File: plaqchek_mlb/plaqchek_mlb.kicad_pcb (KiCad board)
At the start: 2 copper layers, 55 x 71 mm, 46 parts, among them J1 Conn_01x04, J2 Conn_01x04, J3 Conn_01x02, J5 Conn_01x04, SW1 SW_Push, SW2 SW_Push, SW3 SW_Push, U1 DHT22

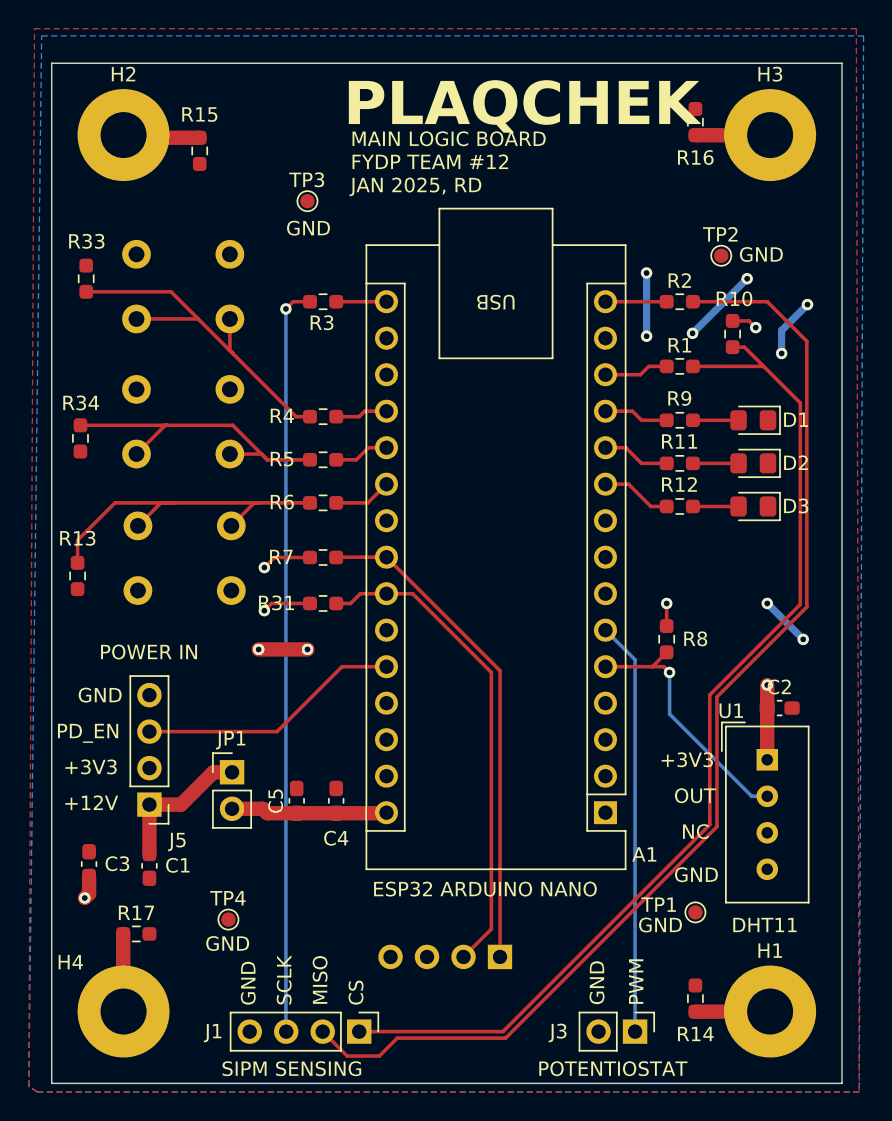
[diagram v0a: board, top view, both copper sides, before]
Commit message: finish potentiostat board, update board constraints
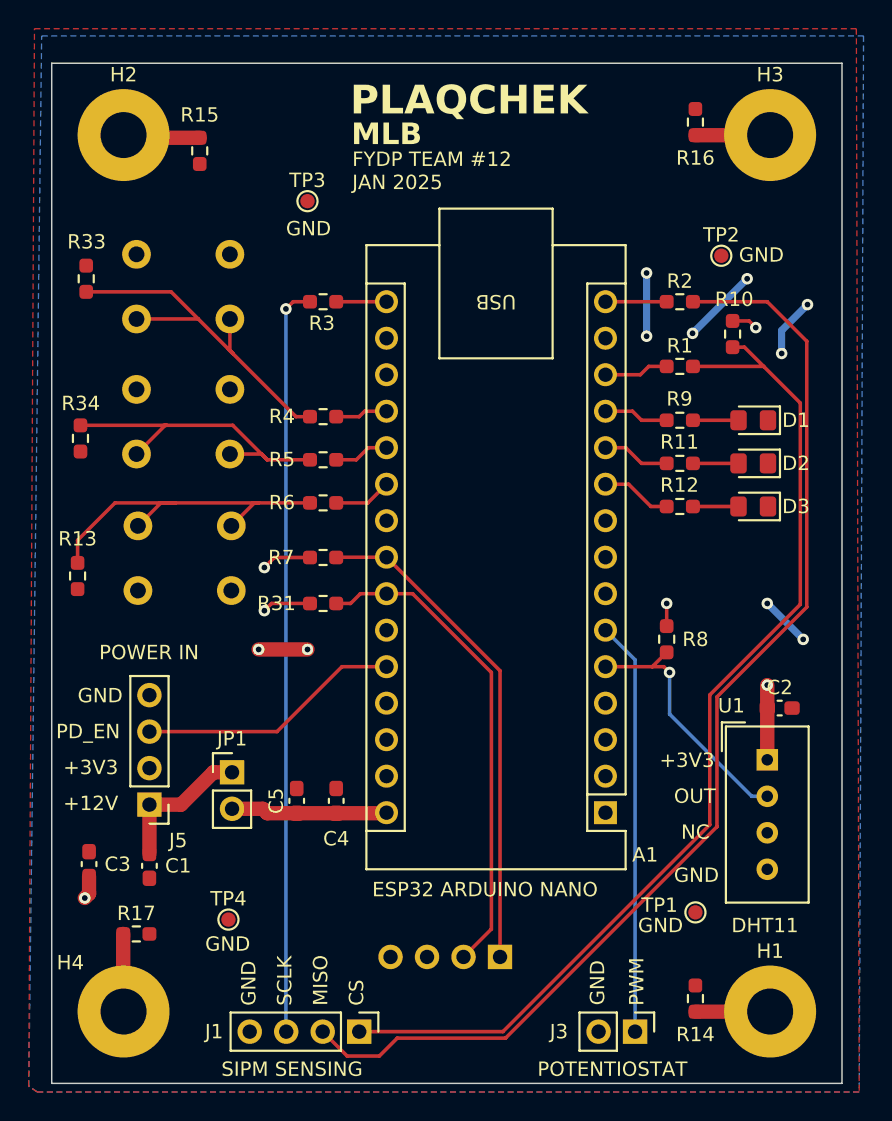
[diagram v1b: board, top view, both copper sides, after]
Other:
- copper layers 2 -> 4
- board text added: "FYDP TEAM #12 JAN 2025"
- board text added: "MLB"

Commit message: finish routing sipm board
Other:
- copper layers 4 -> 2
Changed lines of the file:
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@@
   (layers
     (0 "F.Cu" signal)
-    (1 "In1.Cu" signal)
-    (2 "In2.Cu" signal)
     (31 "B.Cu" signal)
     (32 "B.Adhes" user "B.Adhesive")
@@
       (layer "F.Mask" (type "Top Solder Mask") (thickness 0.01))
       (layer "F.Cu" (type "copper") (thickness 0.035))
-      (layer "dielectric 1" (type "prepreg") (thickness 0.1) (material "FR4") (epsilon_r 4.5) (loss_tangent 0.02))
-      (layer "In1.Cu" (type "copper") (thickness 0.035))
-      (layer "dielectric 2" (type "core") (thickness 1.24) (material "FR4") (epsilon_r 4.5) (loss_tangent 0.02))
-      (layer "In2.Cu" (type "copper") (thickness 0.035))
-      (layer "dielectric 3" (type "prepreg") (thickness 0.1) (material "FR4") (epsilon_r 4.5) (loss_tangent 0.02))
+      (layer "dielectric 1" (type "core") (thickness 1.51) (material "FR4") (epsilon_r 4.5) (loss_tangent 0.02))
       (layer "B.Cu" (type "copper") (thickness 0.035))
       (layer "B.Mask" (type "Bottom Solder Mask") (thickness 0.01))

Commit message: finish all pcbs, generate gerber files
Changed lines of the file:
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@@
       (outputformat 1)
       (mirror false)
-      (drillshape 1)
+      (drillshape 0)
       (scaleselection 1)
-      (outputdirectory "")
+      (outputdirectory "plaqchek_mlb_gerbers/")
     )
   )
@@
     (fp_line (start 1 0.6) (end 1 -0.6)
       (stroke (width 0.1) (type solid)) (layer "F.Fab"))
-    (pad "1" smd roundrect (at -1.025 0 180) (size 1.15 1.4) (layers "F.Cu" "F.Paste" "F.Mask") (roundrect_rratio 0.217391)
+    (pad "1" smd roundrect (at -1.025 0 180) (size 1.15 1.4) (layers "F.Cu" "F.Paste" "F.Mask") (roundrect_rratio 0.2173913043)
       (net 3 "GND") (pinfunction "K") (pintype "passive"))
-    (pad "2" smd roundrect (at 1.025 0 180) (size 1.15 1.4) (layers "F.Cu" "F.Paste" "F.Mask") (roundrect_rratio 0.217391)
+    (pad "2" smd roundrect (at 1.025 0 180) (size 1.15 1.4) (layers "F.Cu" "F.Paste" "F.Mask") (roundrect_rratio 0.2173913043)
       (net 33 "Net-(D3-A)") (pinfunction "A") (pintype "passive"))
     (model "${KICAD6_3DMODEL_DIR}/LED_SMD.3dshapes/LED_0805_2012Metric.wrl"
@@
     (fp_line (start 1 0.6) (end 1 -0.6)
       (stroke (width 0.1) (type solid)) (layer "F.Fab"))
-    (pad "1" smd roundrect (at -1.025 0 180) (size 1.15 1.4) (layers "F.Cu" "F.Paste" "F.Mask") (roundrect_rratio 0.217391)
+    (pad "1" smd roundrect (at -1.025 0 180) (size 1.15 1.4) (layers "F.Cu" "F.Paste" "F.Mask") (roundrect_rratio 0.2173913043)
       (net 3 "GND") (pinfunction "K") (pintype "passive"))
-    (pad "2" smd roundrect (at 1.025 0 180) (size 1.15 1.4) (layers "F.Cu" "F.Paste" "F.Mask") (roundrect_rratio 0.217391)
+    (pad "2" smd roundrect (at 1.025 0 180) (size 1.15 1.4) (layers "F.Cu" "F.Paste" "F.Mask") (roundrect_rratio 0.2173913043)
       (net 32 "Net-(D2-A)") (pinfunction "A") (pintype "passive"))
     (model "${KICAD6_3DMODEL_DIR}/LED_SMD.3dshapes/LED_0805_2012Metric.wrl"
@@
     (property "ki_keywords" "mounting hole")
     (attr exclude_from_pos_files)
-    (fp_text reference "H3" (at 0 -4.2) (layer "F.SilkS")
+    (fp_text reference "H3" (at 0.04 4.73) (layer "F.SilkS")
         (effects (font (size 1 1) (thickness 0.153)))
     )
@@
     (property "ki_keywords" "mounting hole")
     (attr exclude_from_pos_files)
-    (fp_text reference "H2" (at 0 -4.2) (layer "F.SilkS")
+    (fp_text reference "H2" (at 0 4.8) (layer "F.SilkS")
         (effects (font (size 1 1) (thickness 0.153)))
     )
@@
     (fp_line (start 1 0.6) (end 1 -0.6)
       (stroke (width 0.1) (type solid)) (layer "F.Fab"))
-    (pad "1" smd roundrect (at -1.025 0 180) (size 1.15 1.4) (layers "F.Cu" "F.Paste" "F.Mask") (roundrect_rratio 0.217391)
+    (pad "1" smd roundrect (at -1.025 0 180) (size 1.15 1.4) (layers "F.Cu" "F.Paste" "F.Mask") (roundrect_rratio 0.2173913043)
       (net 3 "GND") (pinfunction "K") (pintype "passive"))
-    (pad "2" smd roundrect (at 1.025 0 180) (size 1.15 1.4) (layers "F.Cu" "F.Paste" "F.Mask") (roundrect_rratio 0.217391)
+    (pad "2" smd roundrect (at 1.025 0 180) (size 1.15 1.4) (layers "F.Cu" "F.Paste" "F.Mask") (roundrect_rratio 0.2173913043)
       (net 31 "Net-(D1-A)") (pinfunction "A") (pintype "passive"))
     (model "${KICAD6_3DMODEL_DIR}/LED_SMD.3dshapes/LED_0805_2012Metric.wrl"
